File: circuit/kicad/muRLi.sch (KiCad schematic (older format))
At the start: 7 parts, among them J1 MAX4466, J2 OLED_SH1106, J3 LED, J4 MOD Connector, U1 WeMos_D1_mini

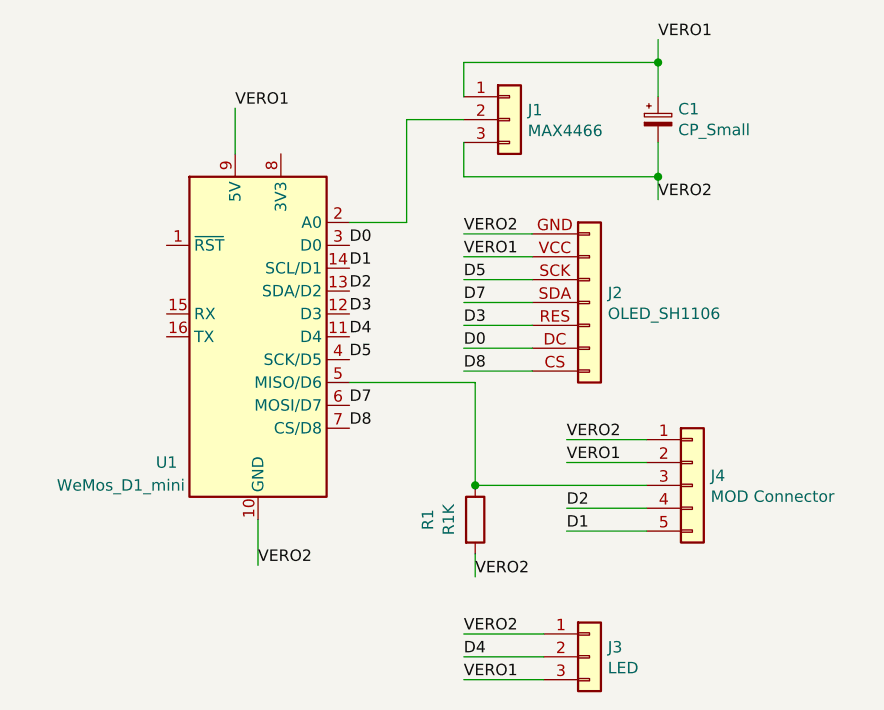
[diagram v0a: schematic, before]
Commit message: Add MOD circuit
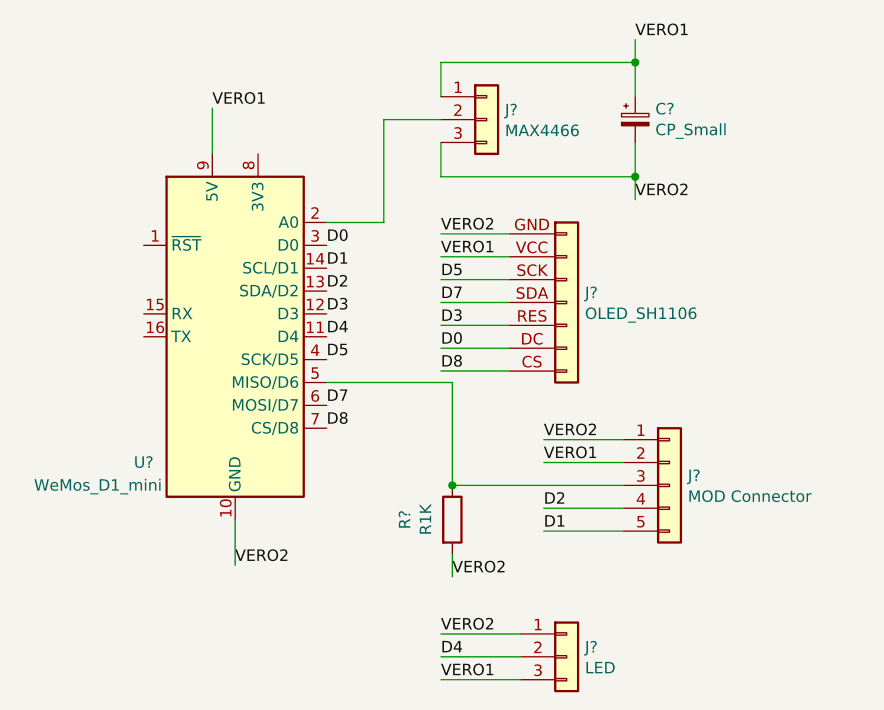
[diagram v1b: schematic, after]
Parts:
- removed C1: CP_Small, symbol Device:CP_Small
- removed J1: MAX4466, symbol Connector_Generic:Conn_01x03
- removed J2: OLED_SH1106, symbol muRLi:OLED_SH1106
- removed J3: LED, symbol Connector_Generic:Conn_01x03
- removed J4: MOD Connector, symbol Connector_Generic:Conn_01x05
- removed R1: R1K, symbol Device:R
- removed U1: WeMos_D1_mini, Module:WEMOS_D1_mini_light, symbol MCU_Module:WeMos_D1_mini
- added C?: CP_Small, symbol Device:CP_Small
- added J?: LED, symbol Connector_Generic:Conn_01x03
- added J?: MOD Connector, symbol Connector_Generic:Conn_01x05
- added J?: MAX4466, symbol Connector_Generic:Conn_01x03
- added J?: OLED_SH1106, symbol muRLi:OLED_SH1106
- added R?: R1K, symbol Device:R
- added U?: WeMos_D1_mini, Module:WEMOS_D1_mini_light, symbol MCU_Module:WeMos_D1_mini
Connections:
- net D0: now also J?.DC, U?.3 (D0)
- net D1: now also J?.5 (Pin_5), U?.14 (SCL/D1)
- net D2: now also J?.4 (Pin_4), U?.13 (SDA/D2)
- net D3: now also J?.RES, U?.12 (D3)
- net D4: now also J?.2 (Pin_2), U?.11 (D4)
- net D5: now also J?.SCK, U?.4 (SCK/D5)
- net D7: now also J?.SDA, U?.6 (MOSI/D7)
- net D8: now also J?.CS, U?.7 (CS/D8)
- net VERO1: now also C?.1, J?.1 (Pin_1), J?.2 (Pin_2), J?.3 (Pin_3), J?.VCC, U?.9 (5V)
- net VERO2: now also C?.2, J?.1 (Pin_1), J?.1 (Pin_1), J?.3 (Pin_3), J?.GND, R?.2, U?.10 (GND)
- new net: J?.3 (Pin_3), R?.1, U?.5 (MISO/D6)
- new net: J?.2 (Pin_2), U?.2 (A0)
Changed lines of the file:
@@
 Comment4 ""
 $EndDescr
+Connection ~ 2450 2750
+Wire Wire Line
+	3200 2750 2450 2750
+Wire Wire Line
+	2450 2300 2450 2750
+Wire Wire Line
+	2450 2300 1900 2300
+Wire Wire Line
+	2450 3050 2450 3150
+Text Label 2450 3150 0    50   ~ 0
+VERO2
 $Comp
-L MCU_Module:WeMos_D1_mini U1
-U 1 1 5EDB5792
-P 1600 2100
-F 0 "U1" H 1200 1550 50  0000 C CNN
-F 1 "WeMos_D1_mini" H 1000 1450 50  0000 C CNN
-F 2 "Module:WEMOS_D1_mini_light" H 1600 950 50  0001 C CNN
-F 3 "https://wiki.wemos.cc/products:d1:d1_mini#documentation" H -250 950 50  0001 C CNN
-	1    1600 2100
+L Device:R R?
+U 1 1 5EE032EB
+P 2450 2900
+F 0 "R?" V 2243 2900 50  0000 C CNN
+F 1 "R1K" V 2334 2900 50  0000 C CNN
+F 2 "" V 2380 2900 50  0001 C CNN
+F 3 "~" H 2450 2900 50  0001 C CNN
+	1    2450 2900
+	1    0    0    -1
+$EndComp
+Text Label 2400 3600 0    50   ~ 0
+VERO1
+Text Label 2400 3400 0    50   ~ 0
+VERO2
+Wire Wire Line
+	2750 3600 2400 3600
+Wire Wire Line
+	2750 3400 2400 3400
+Text Label 1900 2100 0    50   ~ 0
+D4
+Text Label 2400 3500 0    50   ~ 0
+D4
+Wire Wire Line
+	2750 3500 2400 3500
+Text Label 1900 2500 0    50   ~ 0
+D8
+Text Label 2400 2250 0    50   ~ 0
+D8
+Text Label 1900 1700 0    50   ~ 0
+D0
+Text Label 2400 2150 0    50   ~ 0
+D0
+Text Label 1900 2000 0    50   ~ 0
+D3
+Text Label 2400 2050 0    50   ~ 0
+D3
+Text Label 1900 2400 0    50   ~ 0
+D7
+Text Label 2400 1950 0    50   ~ 0
+D7
+Text Label 2400 1850 0    50   ~ 0
+D5
+Wire Wire Line
+	2700 2250 2400 2250
+Wire Wire Line
+	2700 2150 2400 2150
+Wire Wire Line
+	2700 2050 2400 2050
+Wire Wire Line
+	2700 1950 2400 1950
+Wire Wire Line
+	2700 1850 2400 1850
+Text Label 1900 2200 0    50   ~ 0
+D5
+Text Label 1900 1800 0    50   ~ 0
+D1
+Text Label 1900 1900 0    50   ~ 0
+D2
+Text Label 2850 2950 0    50   ~ 0
+D1
+Text Label 2850 2850 0    50   ~ 0
+D2
+Wire Wire Line
+	3200 2950 2850 2950
+Wire Wire Line
+	3200 2850 2850 2850
+Text Label 2850 2650 0    50   ~ 0
+VERO1
+Text Label 2850 2550 0    50   ~ 0
+VERO2
+Wire Wire Line
+	3200 2650 2850 2650
+Wire Wire Line
+	3200 2550 2850 2550
+Wire Wire Line
+	2400 1650 2700 1650
+Wire Wire Line
+	2400 1750 2700 1750
+Text Label 2400 1750 0    50   ~ 0
+VERO1
+Text Label 2400 1650 0    50   ~ 0
+VERO2
+Text Label 1500 3100 0    50   ~ 0
+VERO2
+Wire Wire Line
+	1500 2900 1500 3100
+Text Label 3250 1500 0    50   ~ 0
+VERO2
+Text Label 3250 800  0    50   ~ 0
+VERO1
+Connection ~ 3250 900
+Wire Wire Line
+	3250 900  3250 800
+Connection ~ 3250 1400
+Wire Wire Line
+	3250 1400 3250 1500
+Wire Wire Line
+	3250 1400 3250 1250
+Wire Wire Line
+	2400 1400 3250 1400
+Wire Wire Line
+	2400 1250 2400 1400
+Wire Wire Line
+	3250 900  3250 1050
+Wire Wire Line
+	2400 900  3250 900
+Wire Wire Line
+	2400 1050 2400 900
+Wire Wire Line
+	2150 1150 2400 1150
+Wire Wire Line
+	2150 1600 2150 1150
+Wire Wire Line
+	1900 1600 2150 1600
+Text Label 1400 1100 0    50   ~ 0
+VERO1
+Wire Wire Line
+	1400 1300 1400 1100
+$Comp
+L Connector_Generic:Conn_01x03 J?
+U 1 1 5EE03328
+P 2950 3500
+F 0 "J?" H 3030 3542 50  0000 L CNN
+F 1 "LED" H 3030 3451 50  0000 L CNN
+F 2 "" H 2950 3500 50  0001 C CNN
+F 3 "~" H 2950 3500 50  0001 C CNN
+	1    2950 3500
 	1    0    0    -1
 $EndComp
 $Comp
-L muRLi:OLED_SH1106 J2
-U 1 1 5EDD195F
-P 3050 1950
-F 0 "J2" H 3130 1992 50  0000 L CNN
-F 1 "OLED_SH1106" H 3130 1901 50  0000 L CNN
-F 2 "" H 3050 1950 50  0001 C CNN
-F 3 "~" H 3050 1950 50  0001 C CNN
-	1    3050 1950
+L Connector_Generic:Conn_01x05 J?
+U 1 1 5EE0332E
+P 3400 2750
+F 0 "J?" H 3480 2792 50  0000 L CNN
+F 1 "MOD Connector" H 3480 2701 50  0000 L CNN
+F 2 "" H 3400 2750 50  0001 C CNN
+F 3 "~" H 3400 2750 50  0001 C CNN
+	1    3400 2750
 	1    0    0    -1
 $EndComp
 $Comp
-L Connector_Generic:Conn_01x03 J1
-U 1 1 5EDDB27B
-P 2700 1150
-F 0 "J1" H 2780 1192 50  0000 L CNN
-F 1 "MAX4466" H 2780 1101 50  0000 L CNN
-F 2 "" H 2700 1150 50  0001 C CNN
-F 3 "~" H 2700 1150 50  0001 C CNN
-	1    2700 1150
+L Device:CP_Small C?
+U 1 1 5EE03334
+P 3250 1150
+F 0 "C?" H 3338 1196 50  0000 L CNN
+F 1 "CP_Small" H 3338 1105 50  0000 L CNN
+F 2 "" H 3250 1150 50  0001 C CNN
+F 3 "~" H 3250 1150 50  0001 C CNN
+	1    3250 1150
 	1    0    0    -1
 $EndComp
 $Comp
-L Device:CP_Small C1
-U 1 1 5EDDC226
-P 3350 1150
-F 0 "C1" H 3438 1196 50  0000 L CNN
-F 1 "CP_Small" H 3438 1105 50  0000 L CNN
-F 2 "" H 3350 1150 50  0001 C CNN
-F 3 "~" H 3350 1150 50  0001 C CNN
-	1    3350 1150
+L Connector_Generic:Conn_01x03 J?
+U 1 1 5EE0333A
+P 2600 1150
+F 0 "J?" H 2680 1192 50  0000 L CNN
+F 1 "MAX4466" H 2680 1101 50  0000 L CNN
+F 2 "" H 2600 1150 50  0001 C CNN
+F 3 "~" H 2600 1150 50  0001 C CNN
+	1    2600 1150
 	1    0    0    -1
 $EndComp
 $Comp
-L Connector_Generic:Conn_01x05 J4
-U 1 1 5EDDD50B
-P 3500 2750
-F 0 "J4" H 3580 2792 50  0000 L CNN
-F 1 "MOD Connector" H 3580 2701 50  0000 L CNN
-F 2 "" H 3500 2750 50  0001 C CNN
-F 3 "~" H 3500 2750 50  0001 C CNN
-	1    3500 2750
+L muRLi:OLED_SH1106 J?
+U 1 1 5EE03340
+P 2950 1950
+F 0 "J?" H 3030 1992 50  0000 L CNN
+F 1 "OLED_SH1106" H 3030 1901 50  0000 L CNN
+F 2 "" H 2950 1950 50  0001 C CNN
+F 3 "~" H 2950 1950 50  0001 C CNN
+	1    2950 1950
 	1    0    0    -1
 $EndComp
 $Comp
-L Connector_Generic:Conn_01x03 J3
-U 1 1 5EDDE724
-P 3050 3500
-F 0 "J3" H 3130 3542 50  0000 L CNN
-F 1 "LED" H 3130 3451 50  0000 L CNN
-F 2 "" H 3050 3500 50  0001 C CNN
-F 3 "~" H 3050 3500 50  0001 C CNN
-	1    3050 3500
+L MCU_Module:WeMos_D1_mini U?
+U 1 1 5EE03346
+P 1500 2100
+F 0 "U?" H 1100 1550 50  0000 C CNN
+F 1 "WeMos_D1_mini" H 900 1450 50  0000 C CNN
+F 2 "Module:WEMOS_D1_mini_light" H 1500 950 50  0001 C CNN
+F 3 "https://wiki.wemos.cc/products:d1:d1_mini#documentation" H -350 950 50  0001 C CNN
+	1    1500 2100
 	1    0    0    -1
 $EndComp
-Wire Wire Line
-	1500 1300 1500 1100
-Text Label 1500 1100 0    50   ~ 0
-VERO1
-Wire Wire Line
-	2000 1600 2250 1600
-Wire Wire Line
-	2250 1600 2250 1150
-Wire Wire Line
-	2250 1150 2500 1150
-Wire Wire Line
-	2500 1050 2500 900
-Wire Wire Line
-	2500 900  3350 900
-Wire Wire Line
-	3350 900  3350 1050
-Wire Wire Line
-	2500 1250 2500 1400
-Wire Wire Line
-	2500 1400 3350 1400
-Wire Wire Line
-	3350 1400 3350 1250
-Wire Wire Line
-	3350 1400 3350 1500
-Connection ~ 3350 1400
-Wire Wire Line
-	3350 900  3350 800
-Connection ~ 3350 900
-Text Label 3350 800  0    50   ~ 0
-VERO1
-Text Label 3350 1500 0    50   ~ 0
-VERO2
-Wire Wire Line
-	1600 2900 1600 3100
-Text Label 1600 3100 0    50   ~ 0
-VERO2
-Text Label 2500 1650 0    50   ~ 0
-VERO2
-Text Label 2500 1750 0    50   ~ 0
-VERO1
-Wire Wire Line
-	2500 1750 2800 1750
-Wire Wire Line
-	2500 1650 2800 1650
-Wire Wire Line
-	3300 2550 2950 2550
-Wire Wire Line
-	3300 2650 2950 2650
-Text Label 2950 2550 0    50   ~ 0
-VERO2
-Text Label 2950 2650 0    50   ~ 0
-VERO1
-Wire Wire Line
-	3300 2850 2950 2850
-Wire Wire Line
-	3300 2950 2950 2950
-Text Label 2950 2850 0    50   ~ 0
-D2
-Text Label 2950 2950 0    50   ~ 0
-D1
-Text Label 2000 1900 0    50   ~ 0
-D2
-Text Label 2000 1800 0    50   ~ 0
-D1
-Text Label 2000 2200 0    50   ~ 0
-D5
-Wire Wire Line
-	2800 1850 2500 1850
-Wire Wire Line
-	2800 1950 2500 1950
-Wire Wire Line
-	2800 2050 2500 2050
-Wire Wire Line
-	2800 2150 2500 2150
-Wire Wire Line
-	2800 2250 2500 2250
-Text Label 2500 1850 0    50   ~ 0
-D5
-Text Label 2500 1950 0    50   ~ 0
-D7
-Text Label 2000 2400 0    50   ~ 0
-D7
-Text Label 2500 2050 0    50   ~ 0
-D3
-Text Label 2000 2000 0    50   ~ 0
-D3
-Text Label 2500 2150 0    50   ~ 0
-D0
-Text Label 2000 1700 0    50   ~ 0
-D0
-Text Label 2500 2250 0    50   ~ 0
-D8
-Text Label 2000 2500 0    50   ~ 0
-D8
-Wire Wire Line
-	2850 3500 2500 3500
-Text Label 2500 3500 0    50   ~ 0
-D4
-Text Label 2000 2100 0    50   ~ 0
-D4
-Wire Wire Line
-	2850 3400 2500 3400
-Wire Wire Line
-	2850 3600 2500 3600
-Text Label 2500 3400 0    50   ~ 0
-VERO2
-Text Label 2500 3600 0    50   ~ 0
-VERO1
-$Comp
-L Device:R R1
-U 1 1 5EDF5086
-P 2550 2900
-F 0 "R1" V 2343 2900 50  0000 C CNN
-F 1 "R1K" V 2434 2900 50  0000 C CNN
-F 2 "" V 2480 2900 50  0001 C CNN
-F 3 "~" H 2550 2900 50  0001 C CNN
-	1    2550 2900
-	1    0    0    -1
-$EndComp
-Text Label 2550 3150 0    50   ~ 0
-VERO2
-Wire Wire Line
-	2550 3050 2550 3150
-Wire Wire Line
-	2550 2300 2000 2300
-Wire Wire Line
-	2550 2300 2550 2750
-Wire Wire Line
-	3300 2750 2550 2750
-Connection ~ 2550 2750
 $EndSCHEMATC

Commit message: Fix schematics
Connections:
- net VERO1: now also U?.8 (3V3); no longer J?.3 (Pin_3), U?.9 (5V)
- new net LED_VCC: J?.3 (Pin_3), U?.9 (5V)
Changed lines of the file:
@@
 	1    0    0    -1
 $EndComp
-Text Label 2400 3600 0    50   ~ 0
-VERO1
 Text Label 2400 3400 0    50   ~ 0
 VERO2
@@
 Wire Wire Line
 	1900 1600 2150 1600
-Text Label 1400 1100 0    50   ~ 0
+Text Label 1600 1100 0    50   ~ 0
 VERO1
 Wire Wire Line
@@
 	1    0    0    -1
 $EndComp
+Wire Wire Line
+	1600 1300 1600 1100
+Wire Wire Line
+	1400 1100 1200 1100
+Text Label 1200 1100 0    50   ~ 0
+LED_VCC
+Text Label 2400 3600 0    50   ~ 0
+LED_VCC
 $EndSCHEMATC
